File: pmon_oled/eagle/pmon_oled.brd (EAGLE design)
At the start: 60 x 60 mm, 37 parts, among them J1 USB, J2 USB, J4 PINHD-1X3, J5 PINHD-2X3, Q1 16Mhz, U1 LTC2943, U2 FT232RL, U3 LT1764AEQ, U4 ATMEGA328TQFP32

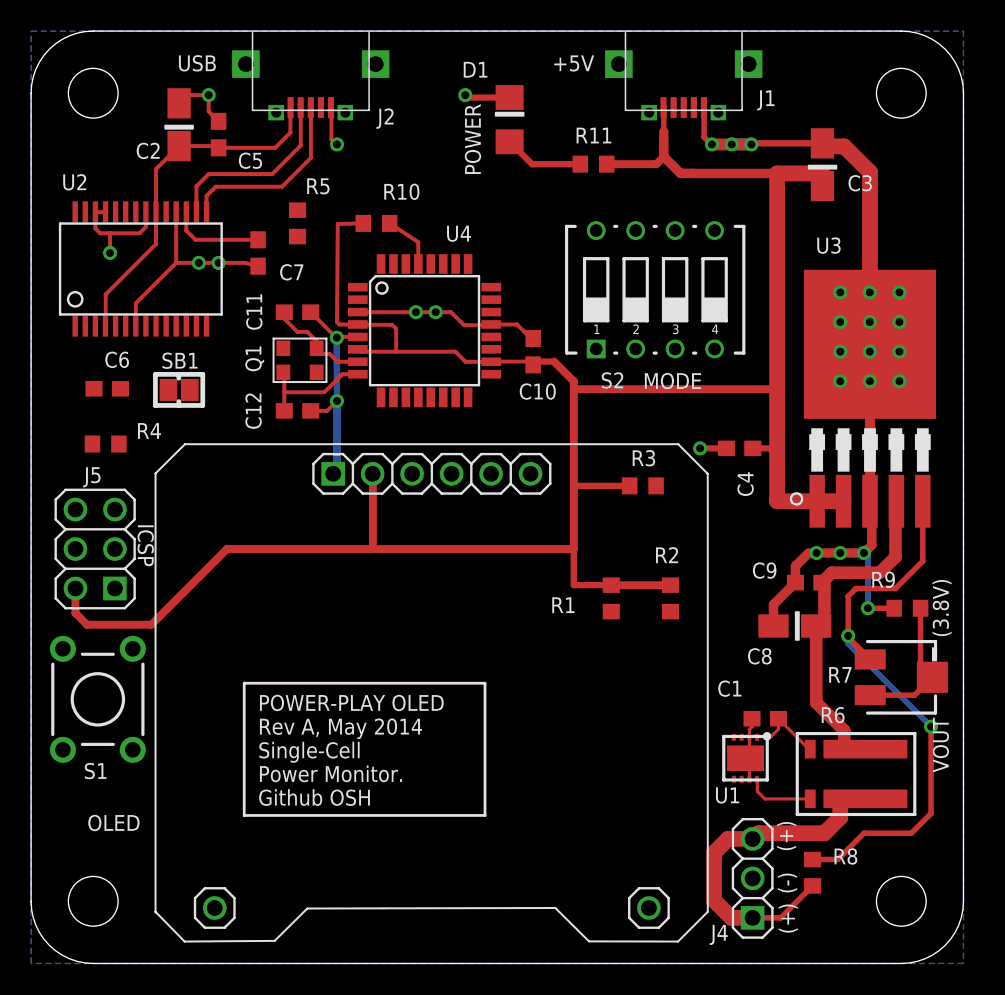
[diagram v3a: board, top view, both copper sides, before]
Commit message: Beefed up a few power traces.
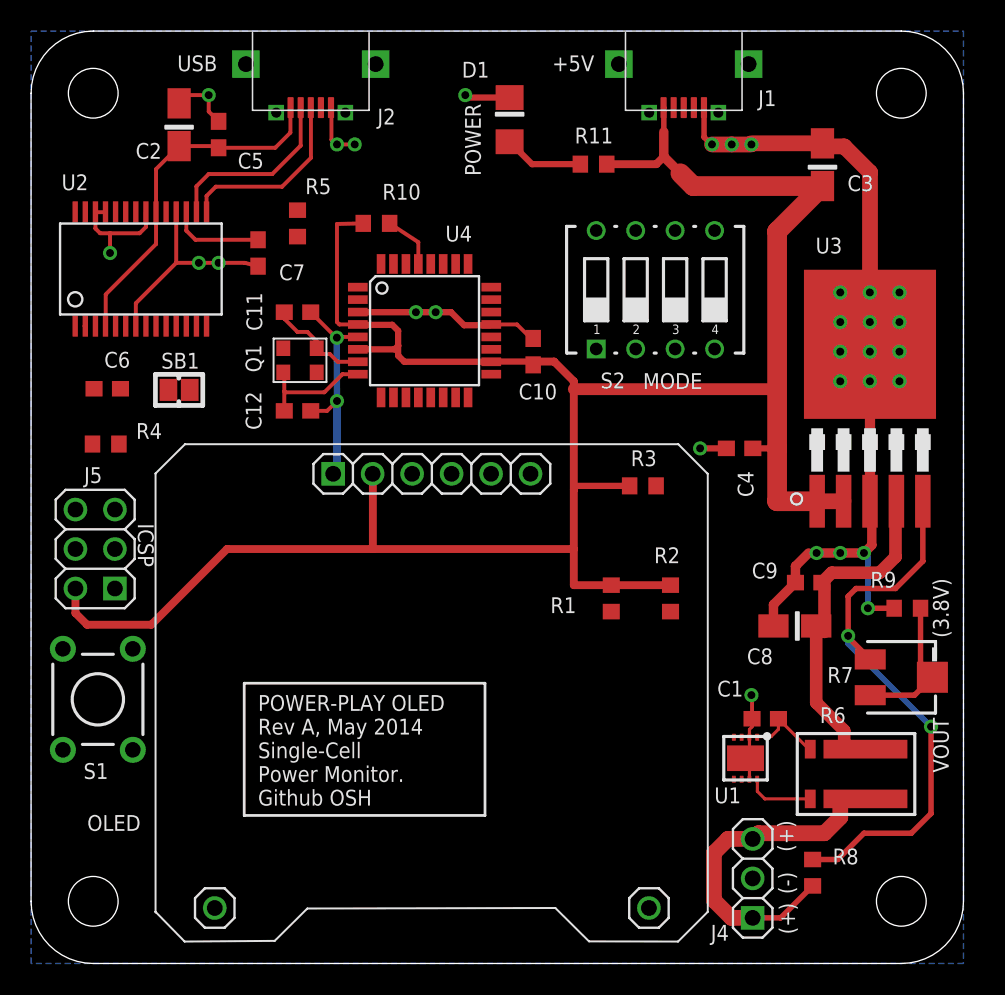
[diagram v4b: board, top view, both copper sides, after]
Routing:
- net GND: track 117.9 -> 120.6 mm, vias 30 -> 32
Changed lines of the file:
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@@
 <wire x1="46.355" y1="52.705" x2="45.085" y2="52.705" width="0.762" layer="16"/>
 <via x="45.085" y="52.705" extent="1-16" drill="0.508"/>
-<wire x1="45.085" y1="52.705" x2="43.815" y2="52.705" width="0.762" layer="1"/>
+<wire x1="45.085" y1="52.705" x2="43.815" y2="52.705" width="1.016" layer="1"/>
 <via x="43.815" y="52.705" extent="1-16" drill="0.508"/>
 <wire x1="43.307" y1="53.174" x2="43.776" y2="52.705" width="0.3556" layer="1"/>
@@
 <wire x1="19.636678125" y1="40.268321875" x2="19.6749375" y2="40.268321875" width="0.254" layer="1"/>
 <wire x1="21.0274" y1="41.92" x2="21.0174" y2="41.91" width="0.254" layer="1"/>
-<wire x1="21.0174" y1="41.91" x2="24.765" y2="41.91" width="0.254" layer="1"/>
-<wire x1="24.765" y1="41.91" x2="26.035" y2="41.91" width="0.254" layer="1"/>
-<wire x1="26.035" y1="41.91" x2="27.0256" y2="41.91" width="0.254" layer="1"/>
+<wire x1="21.0174" y1="41.91" x2="24.765" y2="41.91" width="0.4064" layer="1"/>
+<wire x1="24.765" y1="41.91" x2="26.035" y2="41.91" width="0.4064" layer="1"/>
+<wire x1="26.035" y1="41.91" x2="27.0256" y2="41.91" width="0.4064" layer="1"/>
 <wire x1="29.6126" y1="41.12" x2="29.5644" y2="41.0718" width="0.254" layer="1"/>
-<wire x1="29.5644" y1="41.0718" x2="27.8638" y2="41.0718" width="0.254" layer="1"/>
+<wire x1="29.5644" y1="41.0718" x2="27.8638" y2="41.0718" width="0.4064" layer="1"/>
 <wire x1="29.6126" y1="41.12" x2="31.27" y2="41.12" width="0.254" layer="1"/>
 <wire x1="31.27" y1="41.12" x2="32.17" y2="40.22" width="0.254" layer="1"/>
@@
 <wire x1="5.08" y1="46.99" x2="5.08" y2="45.72" width="0.254" layer="1"/>
 <via x="5.08" y="45.72" extent="1-16" drill="0.508"/>
-<wire x1="27.8638" y1="41.0718" x2="27.0256" y2="41.91" width="0.254" layer="1"/>
+<wire x1="27.8638" y1="41.0718" x2="27.0256" y2="41.91" width="0.4064" layer="1"/>
 <via x="26.035" y="41.91" extent="1-16" drill="0.508"/>
 <via x="24.765" y="41.91" extent="1-16" drill="0.508"/>
@@
 <via x="27.94" y="55.88" extent="1-16" drill="0.508"/>
 <contactref element="S1" pad="A"/>
-<wire x1="45.085" y1="52.705" x2="46.355" y2="52.705" width="0.762" layer="1"/>
-<wire x1="50.927" y1="52.777" x2="46.355" y2="52.777" width="0.4064" layer="1"/>
+<wire x1="45.085" y1="52.705" x2="46.355" y2="52.705" width="1.016" layer="1"/>
+<wire x1="50.927" y1="52.777" x2="46.355" y2="52.777" width="1.016" layer="1"/>
 <wire x1="46.355" y1="52.777" x2="46.355" y2="52.705" width="0.4064" layer="1"/>
 <wire x1="44.743" y1="33.147" x2="43.053" y2="33.147" width="0.4064" layer="1"/>
 <via x="43.053" y="33.147" extent="1-16" drill="0.508"/>
 <wire x1="46.228" y1="14.562" x2="45.724" y2="14.558" width="0" layer="19" extent="1-1"/>
-<wire x1="47.774" y1="21.717" x2="46.394" y2="15.748" width="0" layer="19" extent="1-1"/>
+<wire x1="46.394" y1="15.748" x2="46.394" y2="17.233" width="0.254" layer="1"/>
+<wire x1="46.394" y1="17.233" x2="46.355" y2="17.272" width="0.254" layer="1"/>
+<wire x1="46.355" y1="17.272" x2="45.724" y2="14.558" width="0" layer="19" extent="1-16"/>
+<via x="46.355" y="17.272" extent="1-16" drill="0.508"/>
+<via x="20.828" y="52.705" extent="1-16" drill="0.508"/>
+<wire x1="19.685" y1="52.705" x2="20.828" y2="52.705" width="0.254" layer="1"/>
 </signal>
 <signal name="+5V">
@@
 <wire x1="40.7162" y1="53.5178" x2="40.7162" y2="51.9176" width="0.6096" layer="1"/>
 <wire x1="40.7162" y1="51.9176" x2="41.783" y2="50.8508" width="0.6096" layer="1"/>
-<wire x1="41.783" y1="50.8508" x2="42.605" y2="50.839" width="0.6096" layer="1"/>
 <wire x1="50.584" y1="29.745" x2="52.284" y2="29.745" width="1.016" layer="1"/>
-<wire x1="21.0274" y1="39.52" x2="21.1774" y2="39.37" width="0.254" layer="1"/>
-<wire x1="21.1774" y1="39.37" x2="23.495" y2="39.37" width="0.254" layer="1"/>
-<wire x1="23.495" y1="39.37" x2="27.305" y2="39.37" width="0.254" layer="1"/>
-<wire x1="27.305" y1="39.37" x2="27.955" y2="38.72" width="0.254" layer="1"/>
-<wire x1="27.955" y1="38.72" x2="29.6126" y2="38.72" width="0.254" layer="1"/>
 <wire x1="21.0274" y1="41.12" x2="21.0502" y2="41.0972" width="0.254" layer="1"/>
-<wire x1="21.0502" y1="41.0972" x2="23.241" y2="41.0972" width="0.254" layer="1"/>
-<wire x1="23.241" y1="41.0972" x2="23.495" y2="40.8432" width="0.254" layer="1"/>
-<wire x1="23.495" y1="40.8432" x2="23.495" y2="39.37" width="0.254" layer="1"/>
-<wire x1="21.375" y1="47.625" x2="19.7358" y2="47.586" width="0.254" layer="1"/>
-<wire x1="19.7358" y1="47.586" x2="19.685" y2="41.275" width="0.254" layer="1"/>
+<wire x1="21.0502" y1="41.0972" x2="23.241" y2="41.0972" width="0.4064" layer="1"/>
+<wire x1="23.241" y1="41.0972" x2="23.622" y2="40.7162" width="0.4064" layer="1"/>
+<wire x1="21.375" y1="47.625" x2="19.685" y2="47.586" width="0.254" layer="1"/>
+<wire x1="19.685" y1="47.586" x2="19.685" y2="41.275" width="0.254" layer="1"/>
 <wire x1="19.685" y1="41.275" x2="19.84" y2="41.12" width="0.254" layer="1"/>
 <wire x1="19.84" y1="41.12" x2="21.0274" y2="41.12" width="0.254" layer="1"/>
 <wire x1="29.6126" y1="38.72" x2="29.6276" y2="38.735" width="0.254" layer="1"/>
-<wire x1="29.6276" y1="38.735" x2="32.385" y2="38.735" width="0.254" layer="1"/>
+<wire x1="29.6276" y1="38.735" x2="32.385" y2="38.735" width="0.4064" layer="1"/>
 <wire x1="32.385" y1="38.735" x2="32.3088" y2="38.6588" width="0.254" layer="1"/>
 <wire x1="32.3088" y1="38.6588" x2="32.3088" y2="38.52" width="0.254" layer="1"/>
@@
 <wire x1="34.925" y1="36.957" x2="34.925" y2="30.48" width="0.508" layer="1"/>
 <wire x1="34.925" y1="30.48" x2="34.925" y2="26.67" width="0.508" layer="1"/>
-<wire x1="37.123" y1="24.345" x2="37.338" y2="24.345" width="0.508" layer="1"/>
 <wire x1="37.338" y1="24.345" x2="41.148" y2="24.345" width="0.508" layer="1"/>
 <wire x1="21.98" y1="31.51" x2="21.9964" y2="31.4936" width="0.508" layer="1"/>
@@
 <wire x1="38.52" y1="30.734" x2="34.925" y2="30.734" width="0.4064" layer="1"/>
 <wire x1="34.925" y1="30.734" x2="34.925" y2="30.48" width="0.4064" layer="1"/>
-<wire x1="37.123" y1="24.345" x2="34.925" y2="24.345" width="0.4064" layer="1"/>
-<wire x1="34.925" y1="24.345" x2="34.925" y2="26.67" width="0.4064" layer="1"/>
-<wire x1="32.385" y1="38.735" x2="33.655" y2="38.735" width="0.4064" layer="1"/>
-<wire x1="34.925" y1="36.957" x2="47.879" y2="36.957" width="0.508" layer="1"/>
-<wire x1="42.605" y1="50.839" x2="48.006" y2="50.839" width="0.6096" layer="1"/>
-<wire x1="48.006" y1="50.839" x2="50.927" y2="50.839" width="1.016" layer="1"/>
-<wire x1="50.927" y1="50.839" x2="50.927" y2="50.027" width="0.4064" layer="1"/>
-<wire x1="50.584" y1="29.745" x2="48.006" y2="29.745" width="1.016" layer="1"/>
-<wire x1="48.006" y1="29.745" x2="48.006" y2="33.02" width="1.016" layer="1"/>
-<wire x1="48.006" y1="33.02" x2="48.006" y2="33.147" width="1.016" layer="1"/>
-<wire x1="48.006" y1="33.147" x2="48.006" y2="50.839" width="1.016" layer="1"/>
+<wire x1="37.338" y1="24.345" x2="34.925" y2="24.345" width="0.508" layer="1"/>
+<wire x1="34.925" y1="24.345" x2="34.925" y2="26.67" width="0.508" layer="1"/>
+<wire x1="32.385" y1="38.735" x2="33.655" y2="38.735" width="0.508" layer="1"/>
+<wire x1="34.925" y1="36.957" x2="47.879" y2="36.957" width="0.762" layer="1"/>
+<wire x1="50.584" y1="29.745" x2="48.006" y2="29.745" width="1.27" layer="1"/>
+<wire x1="48.006" y1="29.745" x2="48.006" y2="33.147" width="1.27" layer="1"/>
+<wire x1="48.006" y1="33.147" x2="48.006" y2="47.106" width="1.27" layer="1"/>
 <wire x1="46.443" y1="33.147" x2="48.006" y2="33.147" width="0.4064" layer="1"/>
 <wire x1="47.879" y1="36.957" x2="48.006" y2="36.957" width="0.4064" layer="1"/>
 <wire x1="48.006" y1="36.957" x2="48.006" y2="33.147" width="0.4064" layer="1"/>
+<wire x1="23.622" y1="40.7162" x2="23.622" y2="39.751" width="0.4064" layer="1"/>
+<wire x1="23.622" y1="39.751" x2="23.391" y2="39.52" width="0.4064" layer="1"/>
+<wire x1="23.391" y1="39.52" x2="21.0274" y2="39.52" width="0.4064" layer="1"/>
+<wire x1="23.622" y1="39.751" x2="23.622" y2="39.116" width="0.4064" layer="1"/>
+<wire x1="23.622" y1="39.116" x2="24.018" y2="38.72" width="0.4064" layer="1"/>
+<wire x1="24.018" y1="38.72" x2="29.6126" y2="38.72" width="0.4064" layer="1"/>
+<wire x1="50.927" y1="50.027" x2="42.6068" y2="50.027" width="1.27" layer="1"/>
+<wire x1="42.6068" y1="50.027" x2="41.783" y2="50.8508" width="1.27" layer="1"/>
+<wire x1="48.006" y1="47.106" x2="50.927" y2="50.027" width="1.27" layer="1"/>
 </signal>
 <signal name="RESET">

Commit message: Perfomed auto routing of non critical nets.
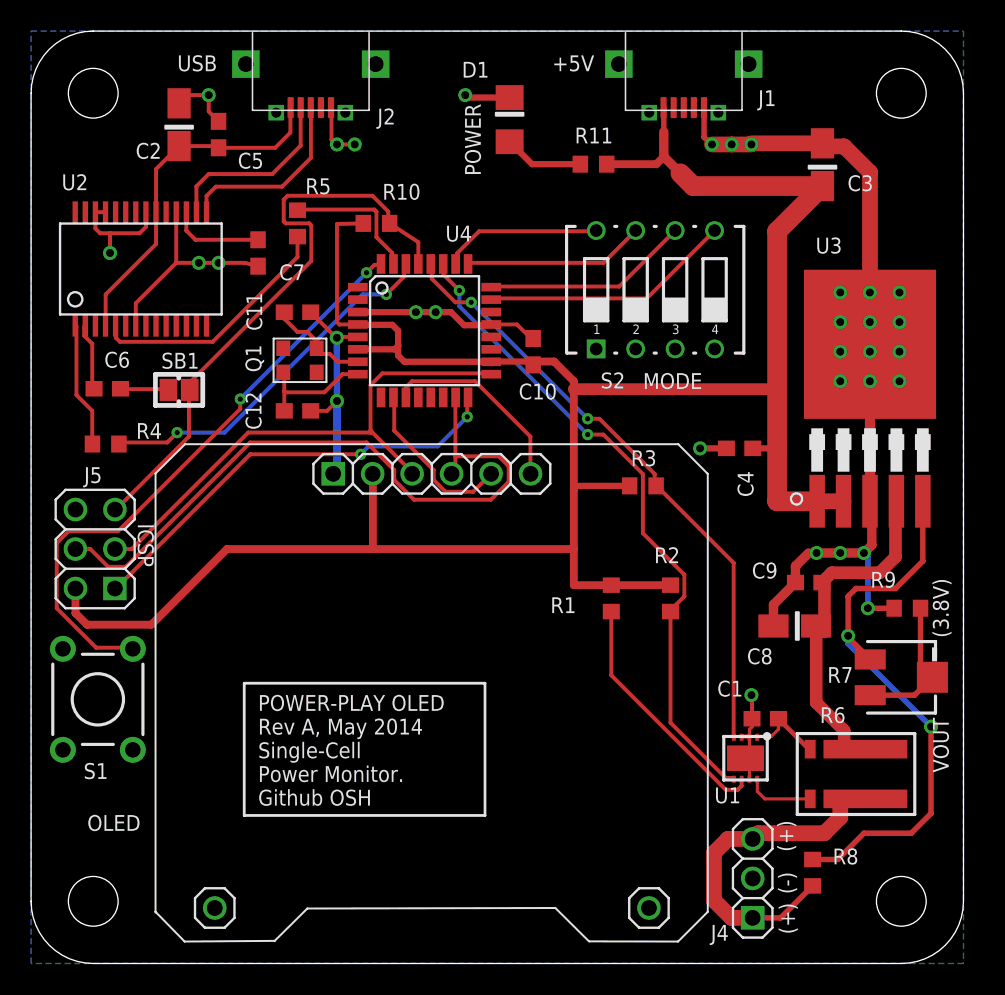
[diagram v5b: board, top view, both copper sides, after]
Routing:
- net MOSI: track 0.00 -> 43.8 mm
- net I2C-DATA: track 0.00 -> 42.5 mm, vias 0 -> 2
- net I2C-CLK: track 0.00 -> 39.6 mm, vias 0 -> 2
- net START: track 0.00 -> 38.9 mm, vias 0 -> 2
- net RESET: track 3.61 -> 38.6 mm
- net SCK: track 0.13 -> 34.7 mm
- net MISO: track 0.00 -> 28.5 mm, vias 0 -> 2
- net SER_RX: track 0.00 -> 23.7 mm, vias 0 -> 2
- net CONFIG4: track 0.00 -> 16.2 mm
- net N$8: track 0.00 -> 16.1 mm
- net N$1: track 0.00 -> 16.1 mm
- net CONFIG3: track 0.00 -> 13.3 mm
- net OLED_D/C: track 0.00 -> 12.7 mm
- net CONFIG2: track 0.00 -> 11.7 mm
- net OLED_RST: track 0.00 -> 10.9 mm
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
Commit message: Changed reset capacitor from 0.01 to 0.1 (to reduce compoent kind count).
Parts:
- C6: value 0.01uF -> 0.1uF
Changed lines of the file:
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@@
 </autorouter>
 <elements>
-<element name="C6" library="pmon_oled" package="C0603" value="0.01uF" x="4.9022" y="36.9824" smashed="yes">
+<element name="C6" library="pmon_oled" package="C0603" value="0.1uF" x="4.9022" y="36.9824" smashed="yes">
 <attribute name="NAME" x="4.70601875" y="38.33854375" size="1.016" layer="25" font="vector" ratio="10"/>
 </element>

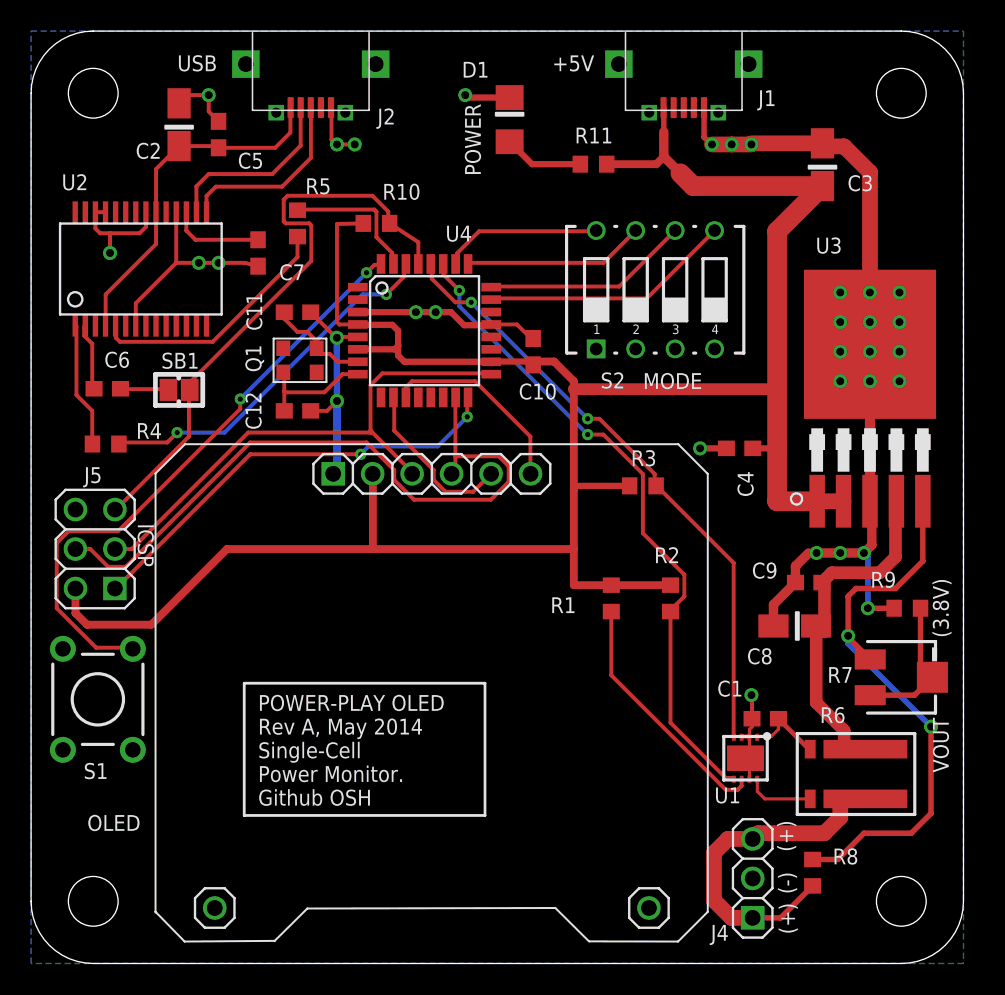
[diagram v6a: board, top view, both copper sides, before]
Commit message: Redesigned the OLED board to pass 5V through rather than regulating to 3.8. This way it can be sued with non instrumeted devices, feeding to the USB input (with some reduce accuracy due to charger standby current and device behavior triggered by the charger in status).
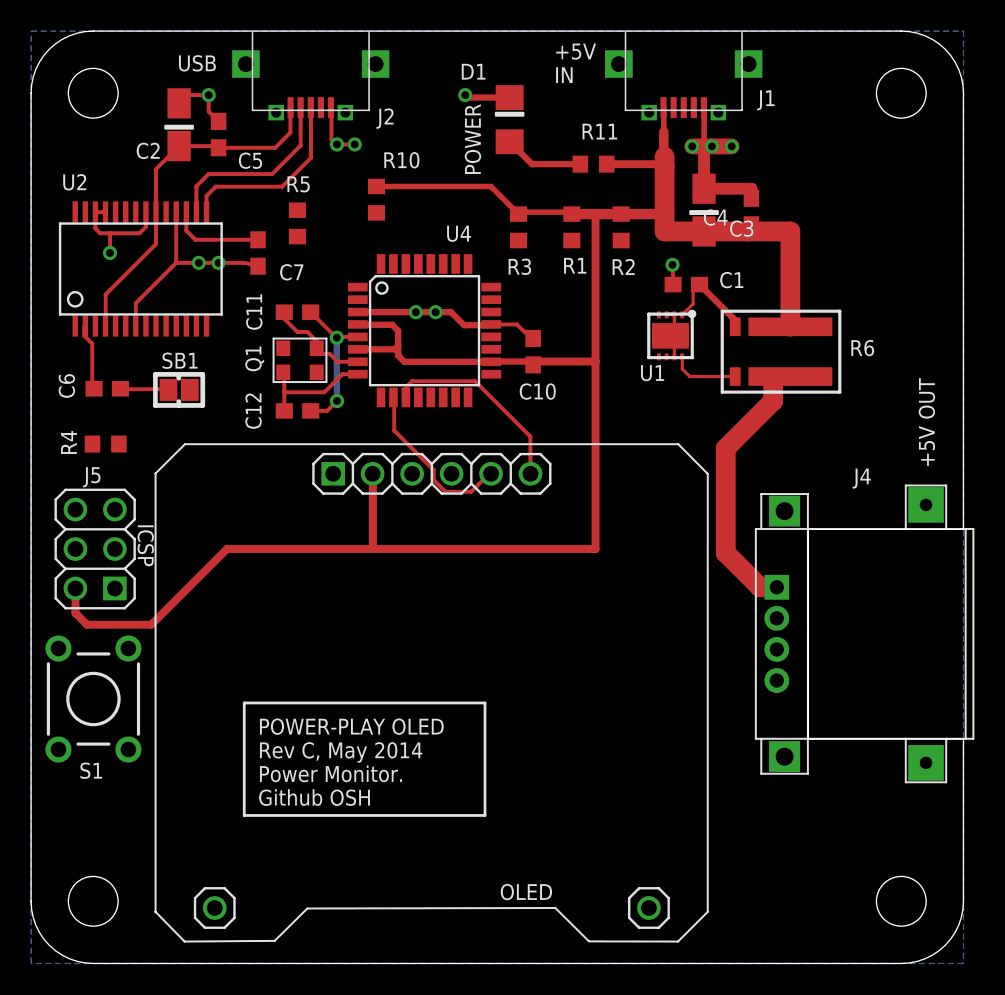
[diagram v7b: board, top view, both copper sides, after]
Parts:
- removed C8: 10uF, pmon_oled:A/3216-18R
- removed C9: 0.1uF, pmon_oled:C0603
- removed R7: 1K, pmon_oled:TRIM-POT_SM-42/43A
- removed R8: 8K2 1%, pmon_oled:R0603
- removed R9: 3K3 1%, pmon_oled:R0603
- removed S2: DIP_SWITCH-X4, pmon_oled:DIP-SWITCH-X4
- removed U3: LT1764AEQ, pmon_oled:TO263-5
- J4: value PINHD-1X3 -> USB_A; device pmon_oled:1X03 -> pmon_oled:USB_A
- moved C1 28.4 mm to (42.2, 43.7)
- moved U1 27.6 mm to (41.1, 40.4)
- moved R6 27.6 mm to (51.6, 39.4)
- moved R2 24.1 mm to (38.0, 47.4)
- moved R1 24.0 mm to (34.8, 47.4)
- moved R3 18.5 mm to (31.4, 47.4), turned to 90 degrees
- moved J4 15.9 mm to (48.5, 21.2)
- moved C4 15.3 mm to (46.4, 48.4), turned to 90 degrees
- moved C3 8.16 mm to (43.3, 48.5)
- moved R10 1.52 mm to (22.2, 49.1), turned to 90 degrees
- moved S1 0.29 mm to (4.01, 17.0)
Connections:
- removed net CONFIG1: S2.8, U4.26
- removed net CONFIG2: S2.7, U4.25
- removed net CONFIG3: S2.6, U4.24
- removed net CONFIG4: S2.5, U4.23
- removed net N$18: R7.1, R7.2, R9.1
- removed net N$19: R7.3, R8.2, U3.5
- removed net N$9: C8.+, C9.1, R6.I2, U3.4
- new net N$4: J4.2, J4.3
- net +5V: now also R6.I2; no longer U3.1, U3.2
- net GND: now also J4.4; no longer C8.-, C9.2, J4.2, R9.2, S2.1, S2.2, S2.3, S2.4, U3.3, U3.6
- net N$22: no longer J4.3, R8.1
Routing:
- net GND: track 121.1 -> 72.2 mm, vias 32 -> 15
- net MOSI: track 43.8 -> 0.11 mm
- net I2C-DATA: track 42.5 -> 0.00 mm, vias 2 -> 0
- net I2C-CLK: track 39.6 -> 0.13 mm, vias 2 -> 0
- net START: track 38.9 -> 0.00 mm, vias 2 -> 0
- net RESET: track 38.6 -> 0.00 mm
- net N$19: track 36.7 -> 0.00 mm, vias 2 -> 0
- net SCK: track 34.7 -> 0.30 mm
- net MISO: track 28.5 -> 0.12 mm, vias 2 -> 0
- net SER_RX: track 23.7 -> 0.00 mm, vias 2 -> 0
- net N$9: track 22.8 -> 0.00 mm
- net +5V: track 155.1 -> 133.1 mm
- net CONFIG4: track 16.2 -> 0.00 mm
- net N$8: track 16.1 -> 0.00 mm
- net N$1: track 16.1 -> 0.05 mm
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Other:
- outline, holes or cut-outs redrawn
- board text added: "+5V IN"
- board text added: "+5V OUT"
- board text added: "POWER-PLAY OLED Rev C, May 2014 Power Monitor. Github OSH"
- board text removed: "(+)"
- board text removed: "(-)"
- board text removed: "(3.8V)"
- board text removed: "+5V"
- board text removed: "MODE"
- board text removed: "POWER-PLAY OLED Rev A, May 2014 Single-Cell Power Monitor. Github OSH"
- board text removed: "VOUT"
